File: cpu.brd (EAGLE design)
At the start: 36.5 x 16.5 mm, 24 parts, among them Q1 DMG2307LSOT23, U1 OPA2340EA/250, X1 ED060SC4_EINK, X2 PIIKKIRIMA-5

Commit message: Schematic should be complete
Schematic should have all parts now
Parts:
- removed D1: STM32L151VBT6, ST Microelctronics_By_element14_Batch_1:QFP50P1600X1600X160-100N
- added C10, C11, C12, C13, C8, C9: (no value), rcl:C0603
- added C14, C15, C18, C19, C20, C21, C7: (no value), rcl:C0805
- added C16, C17: 47n, rcl:C0805
- added E1, E2, E3: TB_ROUND, OMAT_IC:TB_8MM_ROUND
- added H1, H2, H3, H4, H5: (no value), OMAT_IC:CHIP-LED0603
- added N4: MCP1700T-3302E/TT, Microchip_By_element14_Batch_1:SOT95P237X112-3N
- added N5: MAX412CPAMSOP, OMAT_IC:SOP65P490X110-8N
- added Q2: DMG2307LSOT23, OMAT_IC:SOT23
- added R10, R11, R12, R13, R14, R19, R20, R21, R22, R23, R24, R25, R26, R27, R28, R29, R30, R31, R8, R9: (no value), rcl:R0603
- added R15, R32: 5k11, rcl:R0603
- added R16, R17, R18: 22R, rcl:R0603
- added U$1: ADP5063, OMAT_IC:QFN50P400X400X80-21N
- added U$2: DAFUG, dafug:DAFUG
- added X3, X7, X8, X9: PIIKKIRIMA-2, OMAT_IC:PIIKKIRIMA-2
- added X4: 629105136821, OMAT_IC:629105136821
- added X5: 693071010811, OMAT_IC:693071010811
- added X6: PIIKKIRIMA-6, OMAT_IC:PIIKKIRIMA-6
- U1: value OPA2340EA/250 -> STM32L151R8T6; device OMAT_IC:SOP65P490X110-8N -> ST Microelctronics_By_element14_Batch_1:QFP50P1200X1200X160-64N
- moved U1 99.3 mm to (-11.3, -54.0), flipped to the top
- moved R1 5.67 mm to (14.0, 6.99), turned to 0 degrees
- moved X2 1.93 mm to (40.4, 6.10)
- moved Q1 1.52 mm to (14.0, 10.2), turned to 0 degrees
- moved V1 0.46 mm to (22.7, 6.86)
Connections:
- removed net V+: U1.8
- removed net V-: U1.4
- removed net VDDA: D1.22
- removed net VDD_1: D1.50
- removed net VDD_2: D1.75
- removed net VDD_3: D1.100
- removed net VDD_4: D1.28
- removed net VDD_5: D1.11
- removed net VLCD: D1.6
- removed net VSS_5: D1.10
- new net +3V3: C10.1, C11.1, C12.1, C13.1, C15.1, C8.1, C9.1, N4.2, Q2.2, R10.2, R11.1, R12.1, R13.1, R14.1, R27.1, R28.1, R31.2, U1.1, U1.13, U1.19, U1.32, U1.48, U1.64, X3.1, X5.4
- new net +5V: R26.2
- new net BOOT0: R20.2, U1.60, X3.2
- new net CKV: U1.55, X1.33, X1.38
- new net CL: U1.56, X1.5
- new net DACOUT1: R32.1, U1.20
- new net EINKD0: U1.61, X1.12
- new net EINKD1: U1.62, X1.13
- new net EINKD2: U1.29, X1.14
- new net EINKD3: U1.30, X1.15
- new net EINKD4: U1.33, X1.16
- new net EINKD5: U1.34, X1.17
- new net EINKD6: U1.35, X1.18
- new net EINKD7: U1.36, X1.19
- new net G8IO1: R21.1
- new net G8IO2: R22.1
- new net G8IO3: R23.1
- new net G8IO4: C16.1
- new net G9IO1: R24.2, U1.24
- new net G9IO2: C17.1, U1.25
- new net GMODE: U1.27, X1.27, X1.28
- new net LE: U1.57, X1.6
- new net MISO1: U1.22, X5.7
- new net MOSI1: U1.23, X5.3
- new net N$10: H1.A, R11.2
- new net N$12: H1.C, U1.39
- new net N$13: H2.A, R12.2
- new net N$14: H2.C, U1.40
- new net N$15: H3.A, R13.2
- new net N$16: H3.C, U1.51
- new net N$17: H4.A, R14.2
- new net N$18: N5.6, R15.1, R32.2
- new net N$19: H4.C, U1.52
- new net N$20: H5.C, U$1.15
- new net N$21: C19.1, U$1.19
- new net N$22: H5.A, R25.1
- new net N$24: R26.1, U$1.2
- new net N$4: R16.2, X4.2
- new net N$8: N5.3, N5.7, R15.2
- new net NSS1: U1.50, X5.2
- new net OE: U1.58, X1.7
- new net RESETN: R31.1, U1.7, X6.1
- new net RX1: U1.43, X6.6
- new net SCK1: R18.2, X5.5
- new net SCL: R27.2, U$1.1
- new net SDA: R28.2, U$1.17
- new net SPH: U1.59, X1.11
- new net SPV/BOOT1: R19.2, U1.28, X1.32, X1.37
- new net STSCK1: R18.1, U1.21
- new net SWCLK: U1.49, X6.4
- new net SWDIO: U1.46, X6.2
- new net TB1: E1.1, R21.2
- new net TB2: E2.1, R22.2
- new net TB3: E3.1, R23.2
- new net TBSHIELD: R24.1
- new net TX1: U1.42, X6.5
- new net USBDM: R16.1, U1.44
- new net USBDP: R17.1, U1.45
- new net USD_DETN: U1.41, X5.10, X5.10B
- new net VBATT: C21.1, R30.1, U$1.12, U$1.13, U$1.14, U$1.4, X7.1
- new net VEINK33: C7.1, Q2.3, X1.4
- new net VEINK33_CTRLN: Q2.1, R10.1, U1.26
- new net VEINKVCOM: N5.1, N5.2, X1.22
- new net VSYS: C14.1, C20.1, N4.3, Q1.2, R1.2, R25.2, R29.2, R30.2, U$1.10, U$1.11, U$1.9
- new net VUSB: C18.1, R29.1, U$1.6, U$1.7, U$1.8, X4.1, X9.1
- net GND: now also C10.2, C11.2, C12.2, C13.2, C14.2, C15.2, C16.2, C17.2, C18.2, C19.2, C20.2, C21.2, C7.2, C8.2, C9.2, N4.1, N5.5, R19.1, R20.1, R8.1, R9.1, U$1.20, X1.29, X1.31, X1.34, X1.8, X4.5, X4.Z1, X4.Z2, X4.Z3, X4.Z4, X5.6, X5.9, X5.9B, X6.3, X7.2, X8.2, X9.2
- net N$2: now also R17.2, X4.3; no longer Q1.2, R1.2
- net VNEG15: now also N5.4, R9.2
- net VPOS15: now also N5.8, R8.2, X1.30, X1.35, X1.36
- net VSSA: now also U1.12; no longer D1.19
- net VSS_1: now also U1.31; no longer D1.49
- net VSS_2: now also U1.47; no longer D1.74
- net VSS_3: now also U1.63; no longer D1.99
- net VSS_4: now also U1.18; no longer D1.27
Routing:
- net GND: track 35.2 -> 61.5 mm
- net VEINK: track 23.5 -> 26.0 mm
- net VNEG20: track 26.1 -> 23.6 mm
- net VSYS: track 0.00 -> 2.17 mm
- net N$2: track 2.17 -> 0.00 mm
- net VNEG15: track 8.12 -> 6.23 mm
- net VPOS22: track 28.4 -> 26.6 mm
- net VPOS15: track 8.06 -> 6.26 mm
- net N$1: track 4.49 -> 5.68 mm
- net VPOS_CTRLN: track 20.4 -> 19.7 mm
- removed copper zone on layer 1, net GND
- removed copper zone on layer 16, net GND
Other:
- board size 36.5 x 16.5 mm -> 76.5 x 46.5 mm
- board text added: "+15V"
- board text added: "+22V"
- board text added: "-15V"
- board text added: "-20V"
- board text added: "GND"

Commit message: Buzzer added
Added smalles affordable buzzer.
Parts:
- added E4: AST7525MATRQ, OMAT_IC:AST7525MATRQ
- added R33, R34: (no value), rcl:R0603
- added V2: DMG2307LSOT23, OMAT_IC:SOT23
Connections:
- removed net VEINK33_CTRLN: Q2.1, R10.1, U1.26
- new net BUZCTRLN: Q2.1, R10.1, R33.1, U1.26, U1.53, V2.1
- new net N$5: E4.3, R34.2
- new net VEINK1: E4.2, V2.3
- net +3V3: now also R33.2, V2.2
- net GND: now also R34.1
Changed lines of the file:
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@@
 <element name="R32" library="rcl" package="R0603" value="5k11" x="-30.6578" y="-256.9972"/>
 <element name="U$2" library="dafug" package="DAFUG" value="DAFUG" x="-34.544" y="-256.794"/>
+<element name="V2" library="OMAT_IC" package="SOT23" value="DMG2307LSOT23" x="-34.9758" y="-263.017"/>
+<element name="R33" library="rcl" package="R0603" value="" x="-35.9918" y="-269.0368"/>
+<element name="R34" library="rcl" package="R0603" value="" x="-44.6278" y="-272.3896"/>
+<element name="E4" library="OMAT_IC" package="AST7525MATRQ" value="AST7525MATRQ" x="-50.3428" y="-266.8778"/>
 </elements>
 <signals>
@@
 <contactref element="N5" pad="5"/>
 <contactref element="X6" pad="3"/>
+<contactref element="R34" pad="1"/>
 <wire x1="-29.3268" y1="-210.0326" x2="-25.1968" y2="-221.107" width="0" layer="19" extent="1-1"/>
 <wire x1="-29.3268" y1="-206.0448" x2="-29.3268" y2="-210.0326" width="0" layer="19" extent="1-1"/>
@@
 <wire x1="69.02" y1="19.893" x2="62.72" y2="17.018" width="0" layer="19" extent="16-16"/>
 <wire x1="70.52" y1="17.018" x2="69.02" y2="19.893" width="0" layer="19" extent="16-16"/>
+<wire x1="-45.3528" y1="-272.3896" x2="-27.7368" y2="-249.9614" width="0" layer="19" extent="1-1"/>
 </signal>
 <signal name="N$3">
@@
 <wire x1="9.6012" y1="-23.7998" x2="9.6012" y2="-23.1648" width="0" layer="19" extent="1-1"/>
 </signal>
-<signal name="VEINK33_CTRLN">
+<signal name="BUZCTRLN">
 <contactref element="Q2" pad="1"/>
 <contactref element="R10" pad="1"/>
 <contactref element="U1" pad="26"/>
-<wire x1="8.3174" y1="-13.7922" x2="-10.5156" y2="-59.6138" width="0" layer="19" extent="1-1"/>
+<contactref element="V2" pad="1"/>
+<contactref element="R33" pad="1"/>
+<contactref element="U1" pad="53"/>
+<wire x1="-9.525" y1="-48.387" x2="-10.5156" y2="-59.6138" width="0" layer="19" extent="1-1"/>
+<wire x1="8.3174" y1="-13.7922" x2="-9.525" y2="-48.387" width="0" layer="19" extent="1-1"/>
 <wire x1="9.083" y1="-8.8724" x2="8.3174" y2="-13.7922" width="0" layer="19" extent="1-1"/>
+<wire x1="-35.9258" y1="-264.117" x2="-10.5156" y2="-59.6138" width="0" layer="19" extent="1-1"/>
+<wire x1="-36.7168" y1="-269.0368" x2="-35.9258" y2="-264.117" width="0" layer="19" extent="1-1"/>
 </signal>
 <signal name="N$8">
@@
 <contactref element="R11" pad="1"/>
 <contactref element="R31" pad="2"/>
+<contactref element="R33" pad="2"/>
+<contactref element="V2" pad="2"/>
 <wire x1="-31.3828" y1="-216.7382" x2="-30.2768" y2="-225.806" width="0" layer="19" extent="1-1"/>
 <wire x1="-31.3828" y1="-213.3854" x2="-31.3828" y2="-216.7382" width="0" layer="19" extent="1-1"/>
 <wire x1="-29.9328" y1="-240.8936" x2="-30.2768" y2="-225.806" width="0" layer="19" extent="1-1"/>
+<wire x1="-34.0258" y1="-264.117" x2="-29.9328" y2="-240.8936" width="0" layer="19" extent="1-1"/>
+<wire x1="-35.2668" y1="-269.0368" x2="-34.0258" y2="-264.117" width="0" layer="19" extent="1-1"/>
 <wire x1="-18.5268" y1="-138.6078" x2="-31.3828" y2="-213.3854" width="0" layer="19" extent="1-1"/>
 <wire x1="-12.2428" y1="-127.762" x2="-18.5268" y2="-138.6078" width="0" layer="19" extent="1-1"/>
@@
 <wire x1="-31.3828" y1="-256.9972" x2="-13.5382" y2="-59.6138" width="0" layer="19" extent="1-1"/>
 </signal>
+<signal name="VEINK1">
+<contactref element="V2" pad="3"/>
+<contactref element="E4" pad="2"/>
+<wire x1="-34.9758" y1="-261.917" x2="-53.4428" y2="-269.9778" width="0" layer="19" extent="1-1"/>
+</signal>
+<signal name="N$5">
+<contactref element="R34" pad="2"/>
+<contactref element="E4" pad="3"/>
+<wire x1="-47.2428" y1="-269.9778" x2="-43.9028" y2="-272.3896" width="0" layer="19" extent="1-1"/>
+</signal>
 </signals>
-<errors>
-</errors>
 </board>
 </drawing>

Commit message: Layout commit 1
First commit with some layout/placement
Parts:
- removed U$1: ADP5063, OMAT_IC:QFN50P400X400X80-21N
- added N6: ADP5063, OMAT_IC:QFN50P400X400X80-21N
- moved E4 335.1 mm to (77.1, 43.1)
- moved R33 330.9 mm to (70.9, 44.1), turned to 180 degrees
- moved R31 327.8 mm to (130.7, 44.5)
- moved R34 327.8 mm to (116.7, 13.0)
- moved U$2 327.8 mm to (126.8, 28.5)
- moved V2 322.0 mm to (70.9, 41.1), turned to 180 degrees
- moved X9 299.7 mm to (16.3, 46.1), turned to 270 degrees
- moved X8 295.9 mm to (21.3, 46.1), turned to 270 degrees
- moved X7 285.7 mm to (26.4, 46.1), turned to 270 degrees
- moved R32 281.9 mm to (49.9, 13.2), turned to 270 degrees
- moved R15 276.0 mm to (49.9, 10.3), turned to 270 degrees
- moved X3 273.1 mm to (92.0, 18.4)
- moved R21 273.1 mm to (104.3, 70.2)
- moved R22 273.1 mm to (104.3, 66.9)
- moved R23 273.1 mm to (104.3, 63.5)
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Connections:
- removed net +5V: R26.2
- net G8IO1: now also U1.8
- net G8IO2: now also U1.9
- net G8IO3: now also U1.10
- net G8IO4: now also U1.11
- net GND: now also N6.20; no longer U$1.20
- net N$20: now also N6.15; no longer U$1.15
- net N$21: now also N6.19; no longer U$1.19
- net N$24: now also N6.2; no longer U$1.2
- net SCL: now also N6.1; no longer U$1.1
- net SDA: now also N6.17; no longer U$1.17
- net VBATT: now also N6.12, N6.13, N6.14, N6.4; no longer U$1.12, U$1.13, U$1.14, U$1.4
- net VSYS: now also N6.10, N6.11, N6.9, R26.2, X8.1; no longer U$1.10, U$1.11, U$1.9
- net VUSB: now also N6.6, N6.7, N6.8; no longer U$1.6, U$1.7, U$1.8
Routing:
- net VBATT: track 0.00 -> 28.0 mm, vias 0 -> 1
- net VSYS: track 2.17 -> 17.3 mm, vias 0 -> 2
- net N$8: track 0.00 -> 10.9 mm
- net VUSB: track 0.00 -> 9.96 mm
- net VNEG15: track 6.23 -> 15.9 mm
- net VEINKVCOM: track 0.00 -> 8.77 mm
- net N$4: track 0.00 -> 8.53 mm, vias 0 -> 1
- net N$2: track 0.00 -> 7.56 mm, vias 0 -> 1
- net VPOS15: track 6.26 -> 13.5 mm
- net GND: track 61.5 -> 67.8 mm, vias 4 -> 9
- net N$18: track 0.00 -> 5.10 mm
- net SCL: track 0.00 -> 5.01 mm
- net SDA: track 0.00 -> 4.86 mm
- net +3V3: track 0.00 -> 3.79 mm
- net N$20: track 0.00 -> 3.27 mm
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- added copper zone on layer 1, net GND
- added copper zone on layer 1, net VBATT
- added copper zone on layer 1, net VSYS
- added copper zone on layer 1, net VUSB
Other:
- board text added: "CHARGE"

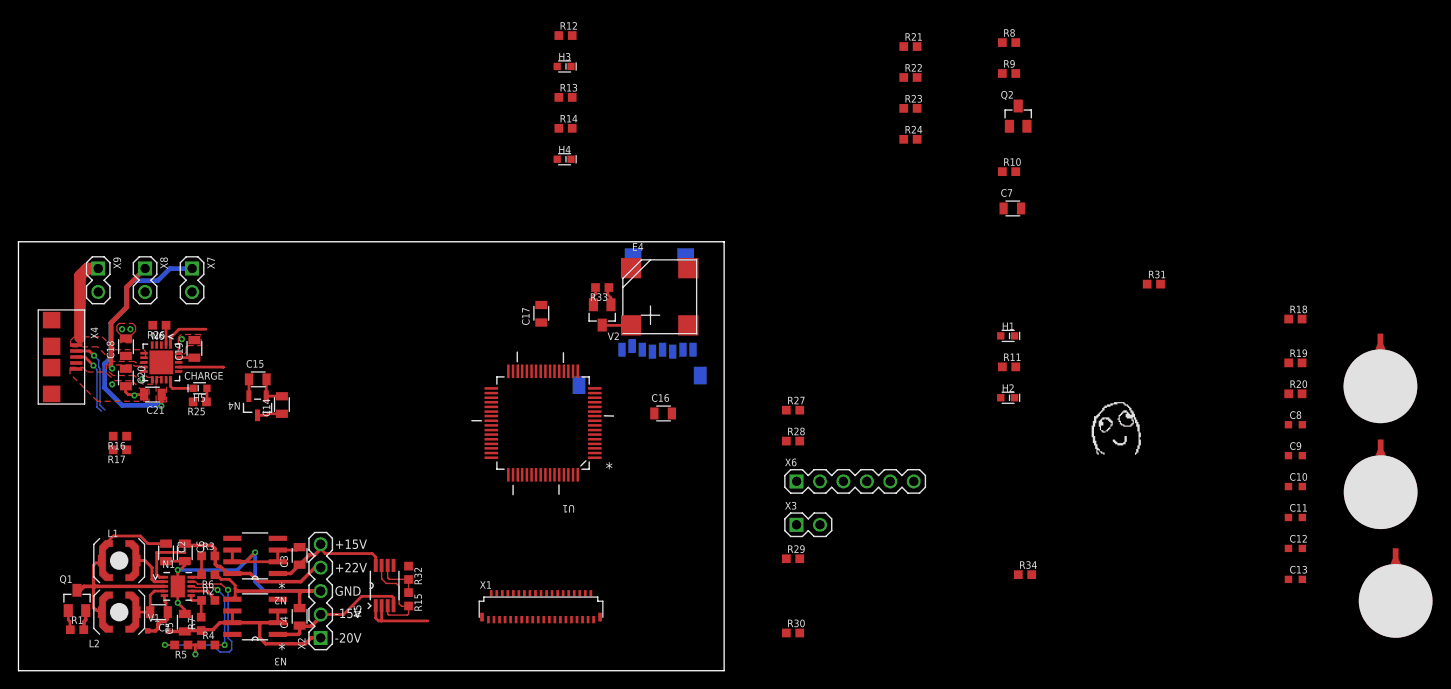
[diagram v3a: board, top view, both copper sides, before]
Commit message: All parts first time onboard - placed
Touchbuttons also prelocated for OSHpark testing
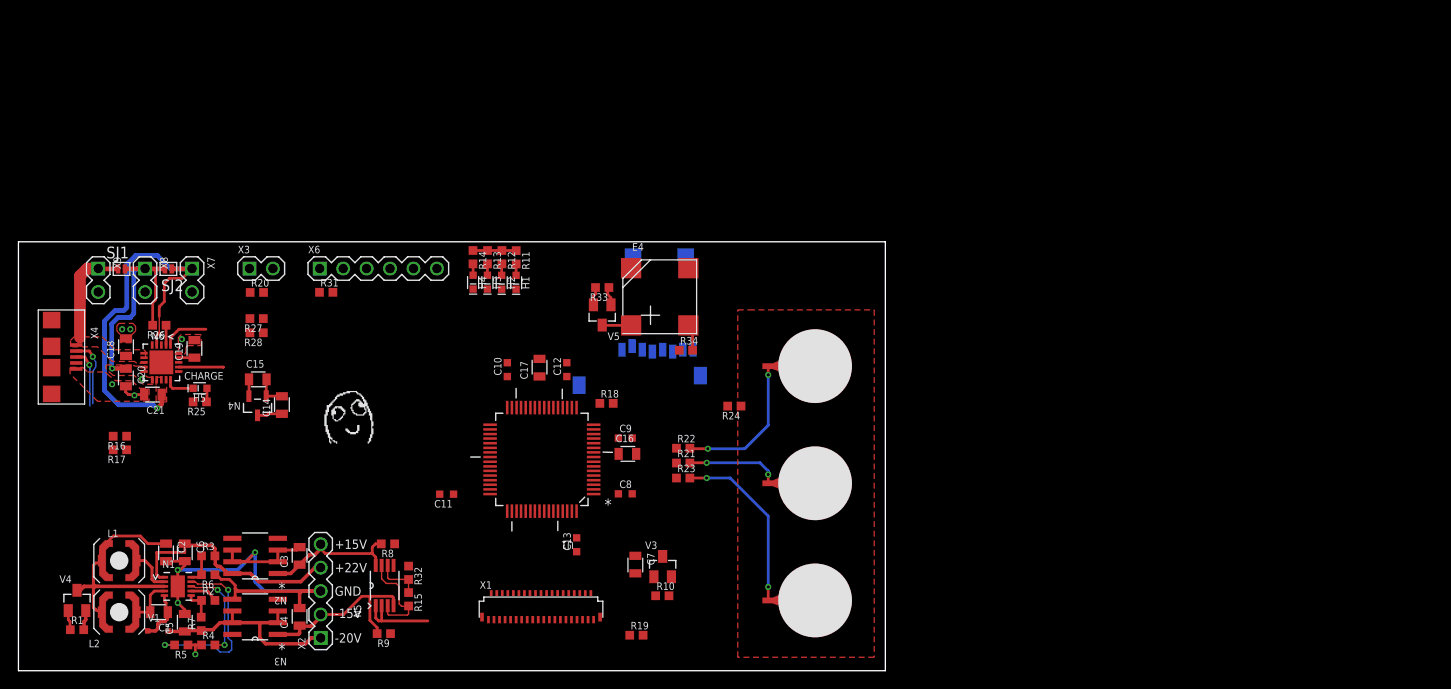
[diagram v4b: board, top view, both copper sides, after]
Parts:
- removed Q2: DMG2307LSOT23, OMAT_IC:SOT23
- removed R29, R30: (no value), rcl:R0603
- added SJ1, SJ2: (no value), OMAT_IC:SJ-SMALL
- added V3: DMG2307LSOT23, OMAT_IC:SOT23
- moved R20 113.1 mm to (33.5, 43.5)
- moved C11 92.0 mm to (54.0, 21.7), turned to 180 degrees
- moved R9 91.0 mm to (47.2, 6.57), turned to 180 degrees
- moved R31 89.7 mm to (41.0, 43.6)
- moved R8 86.5 mm to (47.7, 16.3), turned to 180 degrees
- moved C10 86.4 mm to (60.6, 35.2), turned to 90 degrees
- moved U$2 83.2 mm to (43.6, 29.8)
- moved C12 81.3 mm to (67.1, 35.2), turned to 90 degrees
- moved C13 78.0 mm to (68.1, 16.2), turned to 90 degrees
- moved R19 77.3 mm to (74.6, 6.39)
- moved R18 75.2 mm to (71.4, 31.5)
- moved C8 73.0 mm to (73.4, 21.7)
- moved C9 72.7 mm to (73.4, 27.8)
- moved X3 65.5 mm to (32.7, 46.1)
- moved E3 62.9 mm to (94.0, 10.2), turned to 0 degrees
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- renumbered Q1 to V4, V2 to V5
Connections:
- new net EINKVDDCTRLN: R10.1, U1.26, V3.1
- net +3V3: now also V3.2; no longer Q2.2
- net BUZCTRLN: no longer Q2.1, R10.1, U1.26
- net VBATT: now also SJ2.1; no longer R30.1
- net VEINK33: now also V3.3, X1.30, X1.35, X1.36; no longer Q2.3
- net VPOS15: no longer X1.30, X1.35, X1.36
- net VSYS: now also SJ1.2, SJ2.2; no longer R29.2, R30.2
- net VUSB: now also SJ1.1; no longer R29.1
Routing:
- net TB3: track 0.00 -> 19.3 mm, vias 0 -> 2
- net VBATT: track 28.0 -> 44.4 mm
- net TB2: track 0.00 -> 16.0 mm, vias 0 -> 2
- net VSYS: track 17.3 -> 31.6 mm
- net TB1: track 0.00 -> 10.2 mm, vias 0 -> 2
- net +3V3: track 3.79 -> 8.48 mm
- net VNEG15: track 15.9 -> 20.2 mm
- net N$5: track 0.00 -> 2.89 mm
- net VUSB: track 9.96 -> 12.1 mm
- net VPOS15: track 13.5 -> 15.3 mm
- net N$13: track 0.00 -> 1.25 mm
- net N$17: track 0.00 -> 1.24 mm
- net N$10: track 0.00 -> 1.24 mm
- net N$15: track 0.00 -> 1.24 mm
- net N$2: track 7.56 -> 6.37 mm
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- added copper zone on layer 1, net TBSHIELD
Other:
- board size 76.5 x 46.5 mm -> 94 x 46.5 mm
